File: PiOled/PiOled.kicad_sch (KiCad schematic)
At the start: 10 parts, among them J1 Raspberry_Pi_2_3, J3 OLED, J4 5V_IN, J5 EDM_RDS

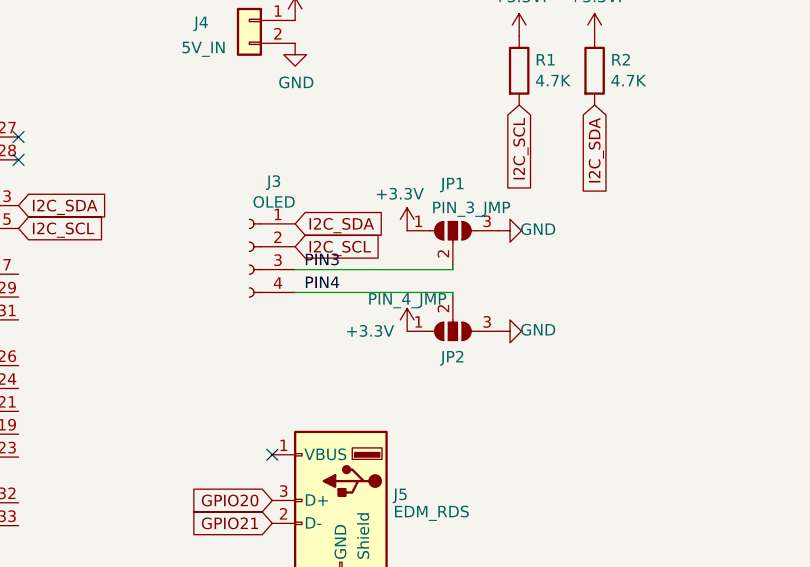
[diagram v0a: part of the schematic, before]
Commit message: add plug in 3 to 4 adapter
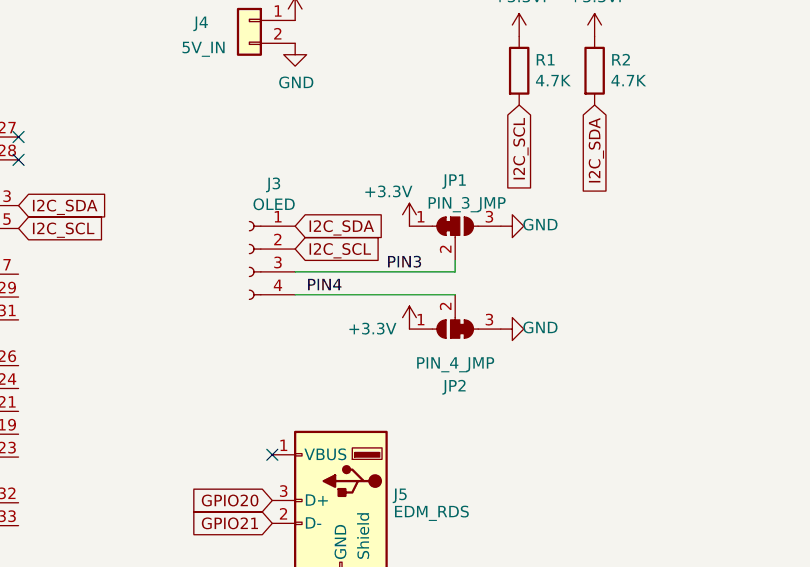
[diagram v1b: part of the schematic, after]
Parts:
- removed JP1: PIN_3_JMP, Jumper:SolderJumper-3_P1.3mm_Open_Pad1.0x1.5mm, symbol PiOled-rescue:SolderJumper_3_Open-Jumper
- removed JP2: PIN_4_JMP, Jumper:SolderJumper-3_P1.3mm_Open_Pad1.0x1.5mm, symbol PiOled-rescue:SolderJumper_3_Open-Jumper
- added JP1: PIN_3_JMP, Scotts:SolderJumper-3_P1mm_Bridged12, symbol Scotts:SolderJumper_3_Bridged12
- added JP2: PIN_4_JMP, Scotts:SolderJumper-3_P1mm_Bridged23, symbol Scotts:SolderJumper_3_Bridged23
- H1, H2: now left out of the parts list
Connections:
- net +3V3: now also JP1.1 (A), JP2.1 (A)
- net GND: now also JP1.3 (B), JP2.3 (B)
- net PIN3: now also JP1.2 (C)
- net PIN4: now also JP2.2 (C)
